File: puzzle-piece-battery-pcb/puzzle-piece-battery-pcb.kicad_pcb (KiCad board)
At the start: 2 copper layers, 27 x 27 mm, 18 parts, among them J1 Lipo, J2 INPUT, J3 OUTPUT, J4 GND Rivet, J5 5V Rivet, J6 3.3V Rivet, U2 MCP73831T-2ACI/OT, U3 LM3480-3.3

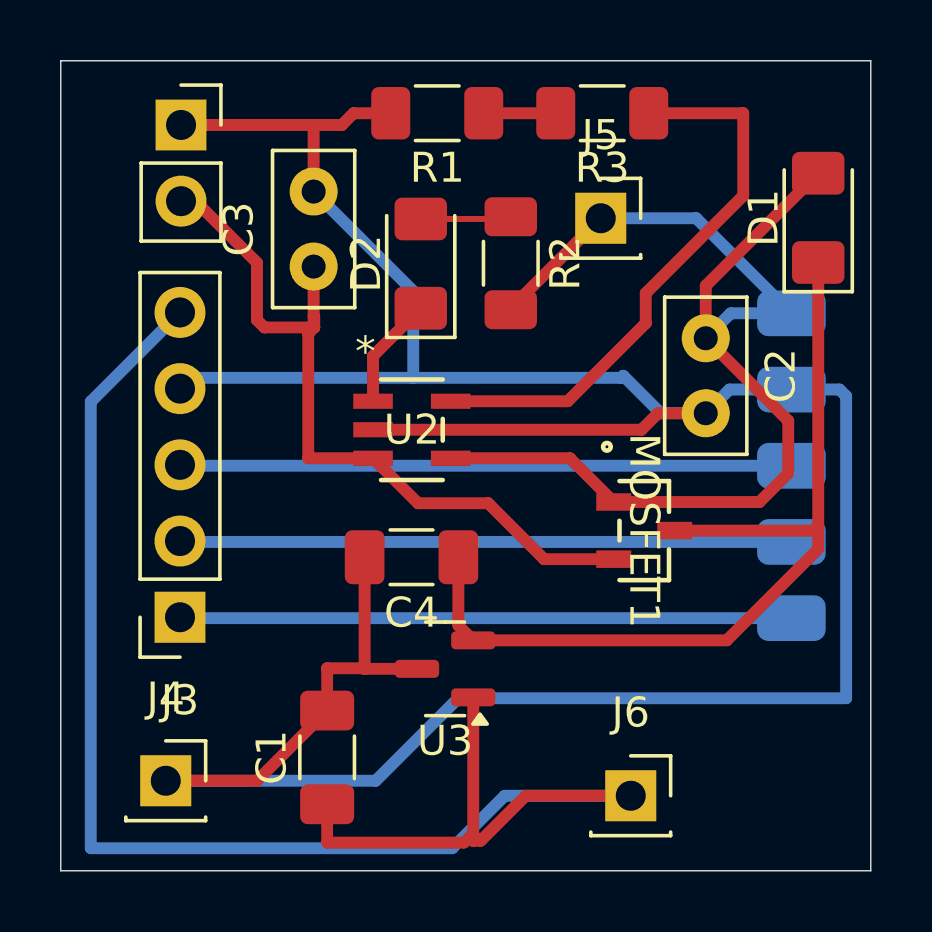
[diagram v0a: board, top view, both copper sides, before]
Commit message: fixed transistor in battery pcb
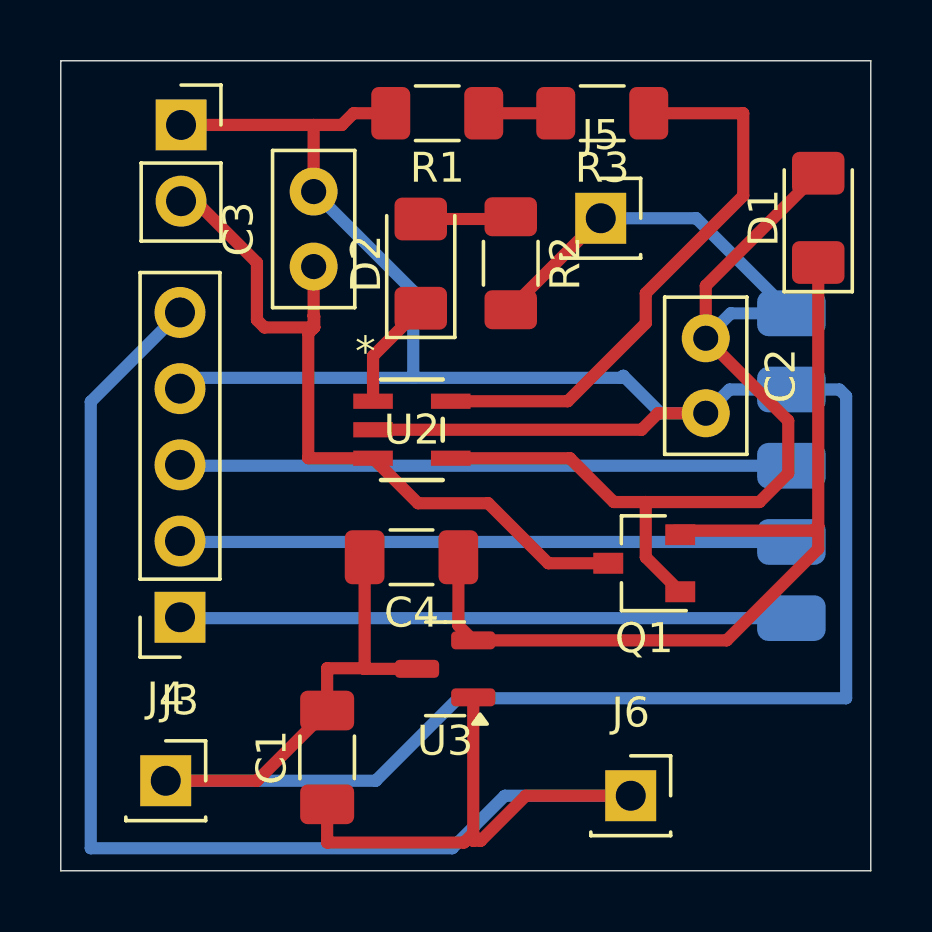
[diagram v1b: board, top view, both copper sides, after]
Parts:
- removed MOSFET1: ZXM61P03FTA, ZXM61P03FTA:SOT23_ZETEX_DIO
- added Q1: Transistor_MOSFET_PCh_SOT23, fab:SOT-23-3, F.Cu at (181.9, 86.2)
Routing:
- net +5V: track 40.3 -> 43.7 mm
